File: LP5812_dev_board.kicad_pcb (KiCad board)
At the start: 2 copper layers, 60 x 60 mm, 34 parts, among them J1 Conn_01x05, U1 LP5812ADSDR, U2 LP5812BDSDR

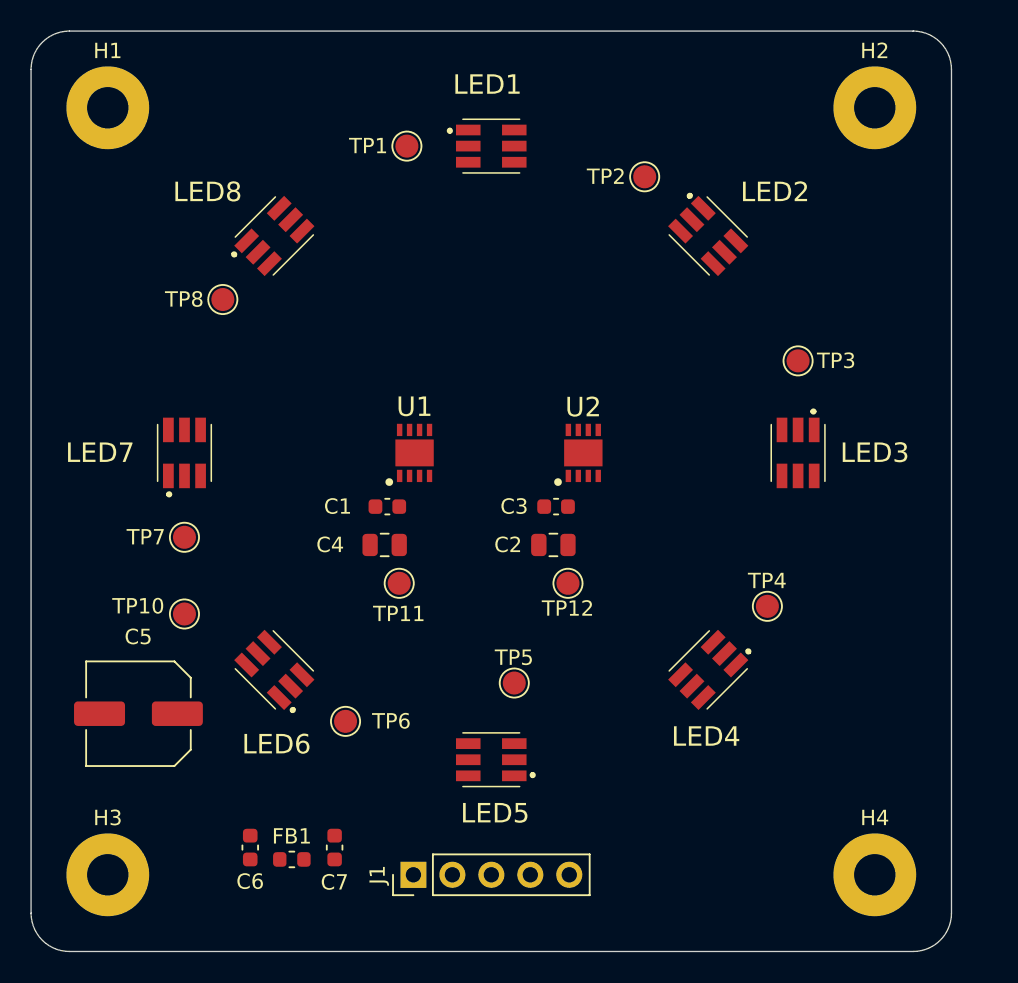
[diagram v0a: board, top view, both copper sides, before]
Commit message: Update LEDS for better reverse bias behavior and cost
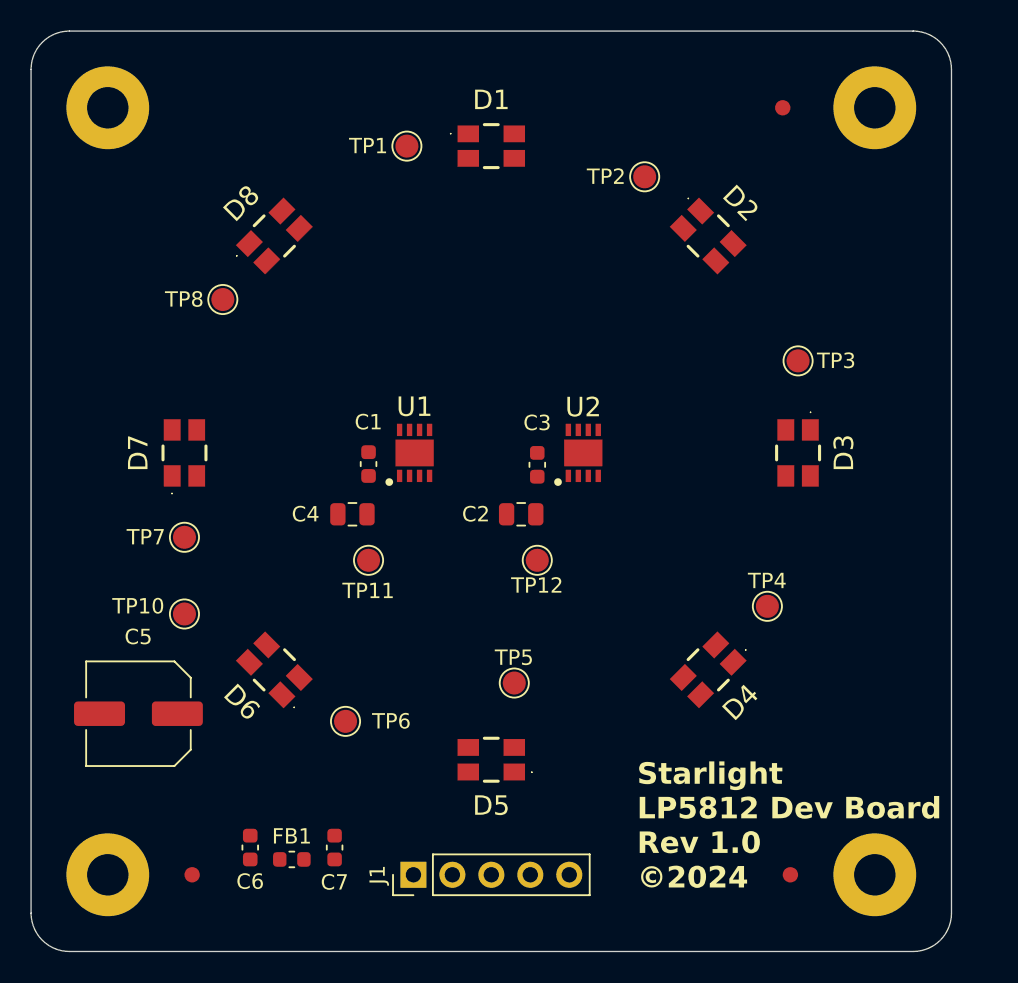
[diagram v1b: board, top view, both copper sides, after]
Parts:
- removed LED1, LED2, LED3, LED4, LED5, LED6, LED7, LED8: ASMB-TTF0-0A20B, ASMB-TTF0-0A20B:ASMBTTF00A20B
- added D1: LED_RABG, CLVBA-FKA-CAEDH8BBB7A363:CLVBAFKACAEDH8BBB7A363, F.Cu at (117.0, 87.5)
- added D2: LED_RABG, CLVBA-FKA-CAEDH8BBB7A363:CLVBAFKACAEDH8BBB7A363, F.Cu at (131.1, 93.4)
- added D3: LED_RABG, CLVBA-FKA-CAEDH8BBB7A363:CLVBAFKACAEDH8BBB7A363, F.Cu at (137.0, 107.5)
- added D4: LED_RABG, CLVBA-FKA-CAEDH8BBB7A363:CLVBAFKACAEDH8BBB7A363, F.Cu at (131.1, 121.6)
- added D5: LED_RABG, CLVBA-FKA-CAEDH8BBB7A363:CLVBAFKACAEDH8BBB7A363, F.Cu at (117.0, 127.5)
- added D6: LED_RABG, CLVBA-FKA-CAEDH8BBB7A363:CLVBAFKACAEDH8BBB7A363, F.Cu at (102.9, 121.6)
- added D7: LED_RABG, CLVBA-FKA-CAEDH8BBB7A363:CLVBAFKACAEDH8BBB7A363, F.Cu at (97.0, 107.5)
- added D8: LED_RABG, CLVBA-FKA-CAEDH8BBB7A363:CLVBAFKACAEDH8BBB7A363, F.Cu at (102.9, 93.4)
- added FID1: ~, Fiducial:Fiducial_1mm_Mask3mm, F.Cu at (136.0, 85.0)
- added FID2: ~, Fiducial:Fiducial_1mm_Mask3mm, F.Cu at (97.5, 135.0)
- added FID3: ~, Fiducial:Fiducial_1mm_Mask3mm, F.Cu at (136.5, 135.0)
- moved C1 3.03 mm to (109.0, 108.2), turned to 90 degrees
- moved C3 2.99 mm to (120.0, 108.3), turned to 90 degrees
- moved C2 2.90 mm to (119.0, 111.5)
- moved C4 2.90 mm to (108.0, 111.5)
- moved TP11 2.50 mm to (109.0, 114.5)
- moved TP12 2.50 mm to (120.0, 114.5)
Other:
- board text added: "Starlight LP5812 Dev Board Rev 1.0 ©2024"
